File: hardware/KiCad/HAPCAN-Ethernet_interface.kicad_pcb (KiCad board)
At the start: 2 copper layers, 86.5 x 33 mm, 13 parts, among them CON1 Connectors CAN bus, IC1 MCP16301HT, U1 HLK-7628N

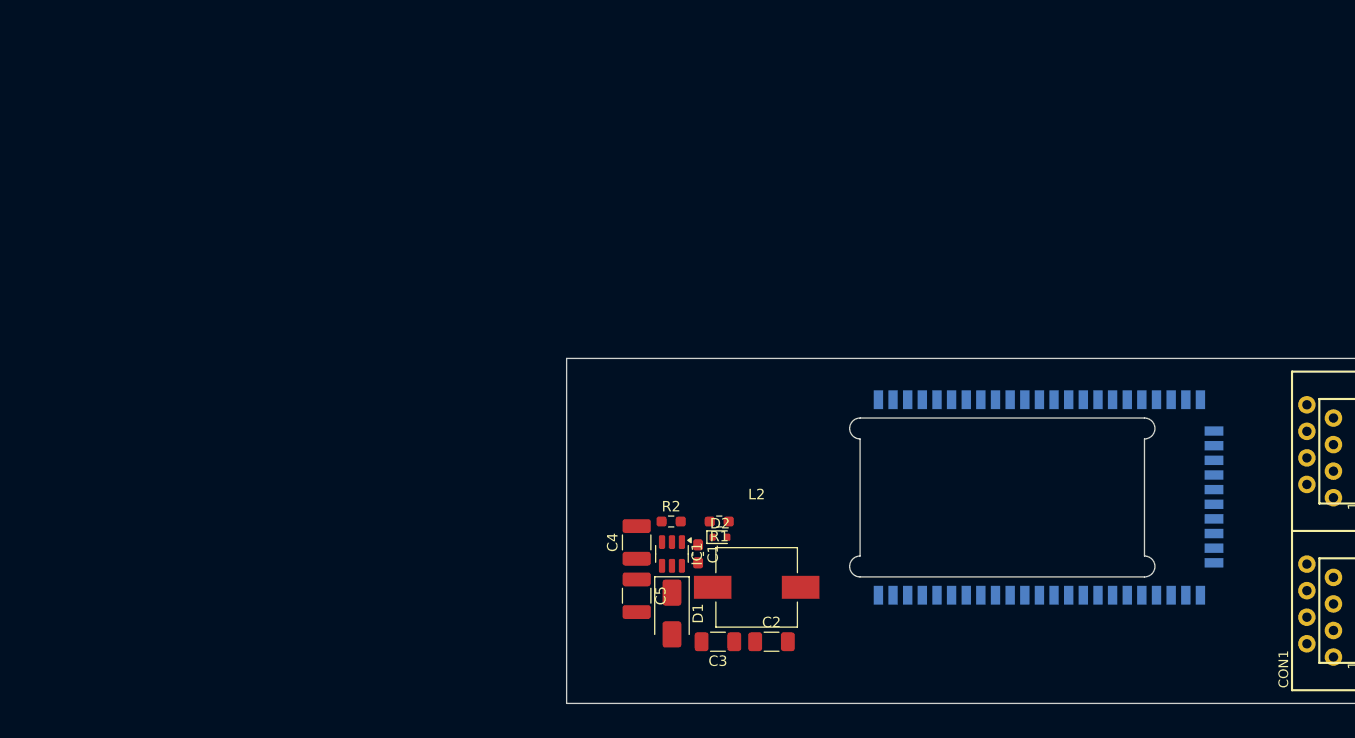
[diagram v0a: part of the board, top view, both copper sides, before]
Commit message: Made some progress in schematic, preliminary component placement on board
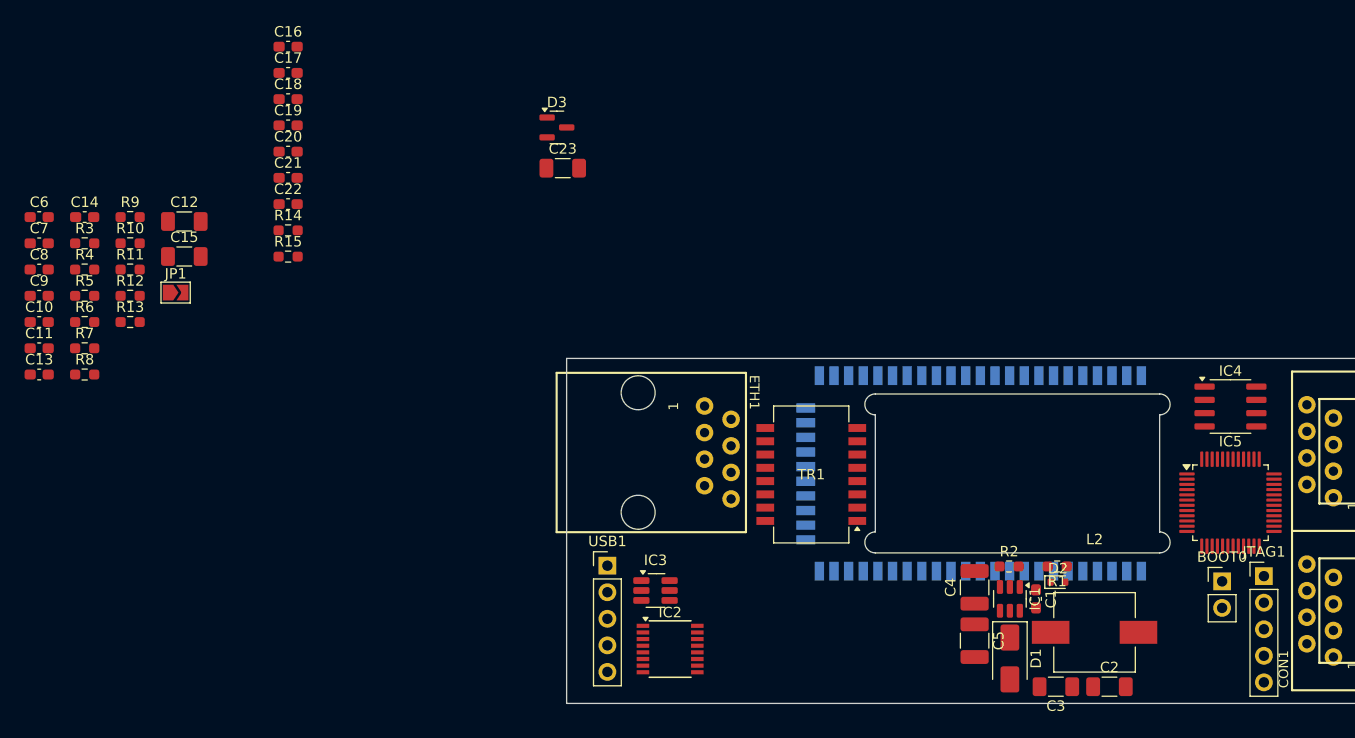
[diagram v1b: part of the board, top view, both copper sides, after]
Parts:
- added BOOT0: Jumper_2_Open, Connector_PinHeader_2.54mm:PinHeader_1x02_P2.54mm_Vertical, F.Cu at (162.7, 121.3)
- added C10: 10n, Capacitor_SMD:C_0603_1608Metric_Pad1.08x0.95mm_HandSolder, F.Cu at (49.5, 96.5)
- added C11: 100n, Capacitor_SMD:C_0603_1608Metric_Pad1.08x0.95mm_HandSolder, F.Cu at (49.5, 99.0)
- added C12: 4.7u, Capacitor_SMD:C_1206_3216Metric_Pad1.33x1.80mm_HandSolder, F.Cu at (63.4, 86.9)
- added C13: 100n, Capacitor_SMD:C_0603_1608Metric_Pad1.08x0.95mm_HandSolder, F.Cu at (49.5, 101.5)
- added C14: 100n, Capacitor_SMD:C_0603_1608Metric_Pad1.08x0.95mm_HandSolder, F.Cu at (53.9, 86.5)
- added C15: 10u, Capacitor_SMD:C_1206_3216Metric_Pad1.33x1.80mm_HandSolder, F.Cu at (63.4, 90.2)
- added C16: 100n, Capacitor_SMD:C_0603_1608Metric_Pad1.08x0.95mm_HandSolder, F.Cu at (73.4, 70.2)
- added C17: 100n, Capacitor_SMD:C_0603_1608Metric_Pad1.08x0.95mm_HandSolder, F.Cu at (73.4, 72.7)
- added C18: 100n, Capacitor_SMD:C_0603_1608Metric_Pad1.08x0.95mm_HandSolder, F.Cu at (73.4, 75.2)
- added C19: 100n, Capacitor_SMD:C_0603_1608Metric_Pad1.08x0.95mm_HandSolder, F.Cu at (73.4, 77.7)
- added C20: 100n, Capacitor_SMD:C_0603_1608Metric_Pad1.08x0.95mm_HandSolder, F.Cu at (73.4, 80.2)
- added C21: 100n, Capacitor_SMD:C_0603_1608Metric_Pad1.08x0.95mm_HandSolder, F.Cu at (73.4, 82.7)
- added C22: 100n, Capacitor_SMD:C_0603_1608Metric_Pad1.08x0.95mm_HandSolder, F.Cu at (73.4, 85.2)
- added C23: 10u 6.3V, Capacitor_SMD:C_1206_3216Metric_Pad1.33x1.80mm_HandSolder, F.Cu at (99.6, 81.8)
- added C6: 330p, Capacitor_SMD:C_0603_1608Metric_Pad1.08x0.95mm_HandSolder, F.Cu at (49.5, 86.5)
- added C7: 47p, Capacitor_SMD:C_0603_1608Metric_Pad1.08x0.95mm_HandSolder, F.Cu at (49.5, 89.0)
- added C8: 47p, Capacitor_SMD:C_0603_1608Metric_Pad1.08x0.95mm_HandSolder, F.Cu at (49.5, 91.5)
- added C9: 100n, Capacitor_SMD:C_0603_1608Metric_Pad1.08x0.95mm_HandSolder, F.Cu at (49.5, 94.0)
- added D3: SZNUP2105L, Package_TO_SOT_SMD:SOT-23, F.Cu at (99.1, 77.9)
- added ETH1: RJ45, ProjectLib:RJ45-PCB-SOCKET, F.Cu at (106.8, 109.0)
- added IC2: FT230XS, Package_SO:SSOP-16_3.9x4.9mm_P0.635mm, F.Cu at (109.9, 127.8)
- added IC3: USBLC6-2SC6, Package_TO_SOT_SMD:SOT-23-6_Handsoldering, F.Cu at (108.5, 122.2)
- added IC4: MCP2561-E-SN, Package_SO:SOIC-8_3.9x4.9mm_P1.27mm, F.Cu at (163.5, 104.6)
- added IC5: STM32F072C8Tx, Package_QFP:LQFP-48_7x7mm_P0.5mm, F.Cu at (163.5, 113.8)
- added JP1: SolderJumper_2_Open, Jumper:SolderJumper-2_P1.3mm_Open_TrianglePad1.0x1.5mm, F.Cu at (62.6, 93.7)
- added JTAG1: Conn_01x05, Connector_PinHeader_2.54mm:PinHeader_1x05_P2.54mm_Vertical, F.Cu at (166.7, 120.8)
- added R10: 27R, Resistor_SMD:R_0603_1608Metric_Pad0.98x0.95mm_HandSolder, F.Cu at (58.2, 89.0)
- added R11: 27R, Resistor_SMD:R_0603_1608Metric_Pad0.98x0.95mm_HandSolder, F.Cu at (58.2, 91.5)
- added R12: 27R, Resistor_SMD:R_0603_1608Metric_Pad0.98x0.95mm_HandSolder, F.Cu at (58.2, 94.0)
- added R13: 27R, Resistor_SMD:R_0603_1608Metric_Pad0.98x0.95mm_HandSolder, F.Cu at (58.2, 96.5)
- added R14: 10k, Resistor_SMD:R_0603_1608Metric_Pad0.98x0.95mm_HandSolder, F.Cu at (73.4, 87.8)
- added R15: 10k, Resistor_SMD:R_0603_1608Metric_Pad0.98x0.95mm_HandSolder, F.Cu at (73.4, 90.3)
- added R3: 1M, Resistor_SMD:R_0603_1608Metric_Pad0.98x0.95mm_HandSolder, F.Cu at (53.9, 89.0)
- added R4: 4k7, Resistor_SMD:R_0603_1608Metric_Pad0.98x0.95mm_HandSolder, F.Cu at (53.9, 91.5)
- added R5: 10k, Resistor_SMD:R_0603_1608Metric_Pad0.98x0.95mm_HandSolder, F.Cu at (53.9, 94.0)
- added R6: 4k7, Resistor_SMD:R_0603_1608Metric_Pad0.98x0.95mm_HandSolder, F.Cu at (53.9, 96.5)
- added R7: 10k, Resistor_SMD:R_0603_1608Metric_Pad0.98x0.95mm_HandSolder, F.Cu at (53.9, 99.0)
- added R8: 27R, Resistor_SMD:R_0603_1608Metric_Pad0.98x0.95mm_HandSolder, F.Cu at (53.9, 101.5)
- added R9: 27R, Resistor_SMD:R_0603_1608Metric_Pad0.98x0.95mm_HandSolder, F.Cu at (58.2, 86.5)
- added TR1: PT61017PEL, Transformer_SMD:Transformer_Ethernet_Bourns_PT61017PEL, F.Cu at (123.4, 111.1)
- added USB1: https://www.aliexpress.com/item/4000926155068.html, Connector_PinHeader_2.54mm:PinHeader_1x05_P2.54mm_Vertical, F.Cu at (103.9, 119.8)
- moved C2 32.6 mm to (151.9, 131.4)
- moved C3 32.6 mm to (146.8, 131.4)
- moved R1 32.6 mm to (146.9, 119.9)
- moved C4 32.6 mm to (139.0, 121.9)
- moved D2 32.6 mm to (147.0, 121.4)
- moved C1 32.6 mm to (144.9, 123.0)
- moved C5 32.6 mm to (139.0, 127.0)
- moved D1 32.6 mm to (142.4, 128.7)
- moved IC1 32.6 mm to (142.4, 123.0)
- moved L2 32.6 mm to (150.5, 126.2)
- moved R2 32.6 mm to (142.3, 119.9)
- moved U1 7.32 mm to (138.9, 111.0), turned to 0 degrees
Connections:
- net Net-(IC1-EN) renamed +24V
- U1 pad 1: Net-(U1-GND-Pad1) -> GND
- U1 pad 15: unconnected-(U1-UART_TXD1-Pad15) -> Net-(U1-UART_TXD1)
- U1 pad 16: unconnected-(U1-UART_RXD1-Pad16) -> Net-(U1-UART_RXD1)
- U1 pad 2: unconnected-(U1-3.3VD-Pad2) -> +3V3
- U1 pad 21: Net-(U1-GND-Pad1) -> GND
- U1 pad 23: Net-(U1-GND-Pad1) -> GND
- U1 pad 3: unconnected-(U1-3.3VD-Pad3) -> +3V3
- U1 pad 31: unconnected-(U1-UART_TXD0-Pad31) -> Net-(U1-UART_TXD0)
- U1 pad 32: unconnected-(U1-UART_RXD0-Pad32) -> Net-(U1-UART_RXD0)
- U1 pad 34: unconnected-(U1-MDI_RP_P0-Pad34) -> /PHY_RX+
- U1 pad 35: unconnected-(U1-MDI_RN_P0-Pad35) -> /PHY_RX-
- U1 pad 36: unconnected-(U1-MDI_TP_P0-Pad36) -> /PHY_TX+
- U1 pad 37: unconnected-(U1-MDI_TN_P0-Pad37) -> /PHY_TX-
- U1 pad 4: Net-(U1-GND-Pad1) -> GND
- U1 pad 56: Net-(U1-GND-Pad1) -> GND

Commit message: Finished schematic, but needs cleanup. Started component placement on board.
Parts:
- removed D2: BAS521-QX, Diode_SMD:D_SOD-523
- added C15: 100n, Capacitor_SMD:C_0603_1608Metric_Pad1.08x0.95mm_HandSolder, B.Cu at (172.5, 117.6)
- added C16: 10u 16V, Capacitor_SMD:C_1210_3225Metric_Pad1.33x2.70mm_HandSolder, F.Cu at (70.3, 167.6)
- added C17: 10u 10V, Capacitor_SMD:C_1210_3225Metric_Pad1.33x2.70mm_HandSolder, F.Cu at (77.3, 160.9)
- added C18: 22u 10V, Capacitor_SMD:C_1210_3225Metric_Pad1.33x2.70mm_HandSolder, F.Cu at (80.6, 160.9)
- added C20: 10n, Capacitor_SMD:C_0603_1608Metric_Pad1.08x0.95mm_HandSolder, F.Cu at (137.0, 183.0)
- added C21: 100n, Capacitor_SMD:C_0603_1608Metric_Pad1.08x0.95mm_HandSolder, F.Cu at (139.5, 183.7)
- added C22: 10u 6.3V, Capacitor_SMD:C_1206_3216Metric_Pad1.33x1.80mm_HandSolder, F.Cu at (135.0, 183.9)
- added C23: 100n, Capacitor_SMD:C_0603_1608Metric_Pad1.08x0.95mm_HandSolder, F.Cu at (137.2, 179.6)
- added C24: 100n, Capacitor_SMD:C_0603_1608Metric_Pad1.08x0.95mm_HandSolder, F.Cu at (145.2, 179.6)
- added C6: 100n, Capacitor_SMD:C_0603_1608Metric_Pad1.08x0.95mm_HandSolder, F.Cu at (57.0, 162.7)
- added C7: 100n, Capacitor_SMD:C_0603_1608Metric_Pad1.08x0.95mm_HandSolder, F.Cu at (67.9, 161.6)
- added C8: 10u 16V, Capacitor_SMD:C_1210_3225Metric_Pad1.33x2.70mm_HandSolder, F.Cu at (70.3, 162.6)
- added FB1: 1k@100MHz, Inductor_SMD:L_0805_2012Metric_Pad1.15x1.40mm_HandSolder, F.Cu at (160.0, 127.9)
- added FB2: 1k@100MHz, Inductor_SMD:L_0805_2012Metric_Pad1.15x1.40mm_HandSolder, F.Cu at (165.2, 131.3)
- added IC3: TLV62568DRL, Package_TO_SOT_SMD:SOT-563, F.Cu at (73.3, 164.2)
- added IC5: MCP3422A0-E/MS, Package_SO:MSOP-8_3x3mm_P0.65mm, F.Cu at (141.2, 181.1)
- added L1: 3.3uH, ProjectLib:SPM7054VT, F.Cu at (63.5, 165.2)
- added NT1: NetTie_2, NetTie:NetTie-2_SMD_Pad0.5mm, F.Cu at (58.9, 155.3)
- added NT2: NetTie_2, NetTie:NetTie-2_SMD_Pad0.5mm, F.Cu at (55.8, 155.3)
- added NT3: NetTie_2, NetTie:NetTie-2_SMD_Pad0.5mm, F.Cu at (83.0, 162.5)
- added NT4: NetTie_2, NetTie:NetTie-2_SMD_Pad0.5mm, F.Cu at (83.0, 161.6)
- added R10: 22k, Resistor_SMD:R_0603_1608Metric_Pad0.98x0.95mm_HandSolder, F.Cu at (146.7, 179.6)
- added R13: 10k, Resistor_SMD:R_0603_1608Metric_Pad0.98x0.95mm_HandSolder, B.Cu at (119.8, 119.9)
- added R14: 10k, Resistor_SMD:R_0603_1608Metric_Pad0.98x0.95mm_HandSolder, B.Cu at (118.3, 119.9)
- added R3: 100k, Resistor_SMD:R_0603_1608Metric_Pad0.98x0.95mm_HandSolder, F.Cu at (73.6, 162.3)
- added R4: 22k, Resistor_SMD:R_0603_1608Metric_Pad0.98x0.95mm_HandSolder, F.Cu at (73.6, 160.8)
- added R7: 330k, Resistor_SMD:R_0603_1608Metric_Pad0.98x0.95mm_HandSolder, F.Cu at (134.2, 179.6)
- added R8: 22k, Resistor_SMD:R_0603_1608Metric_Pad0.98x0.95mm_HandSolder, F.Cu at (135.7, 179.6)
- added R9: 22k, Resistor_SMD:R_0603_1608Metric_Pad0.98x0.95mm_HandSolder, F.Cu at (148.2, 179.6)
- added TVS1: P6SMB33CA, Diode_SMD:D_SMB_Handsoldering, F.Cu at (166.9, 125.3)
- C2: value 10u 6.3V -> 100n; footprint Capacitor_SMD:C_1206_3216Metric_Pad1.33x1.80mm_HandSolder -> Capacitor_SMD:C_0603_1608Metric_Pad1.08x0.95mm_HandSolder
- C3: value 10u 6.3V -> 10u 10V
- C35: renamed from C6; moved to B.Cu
- D1: value B140Q -> US1D; footprint Diode_SMD:D_SMA -> Diode_SMD:D_SMA_Handsoldering
- IC1: value MCP16301HT -> LMR51430Y
- L2: value 15uH -> 1uH; footprint Inductor_SMD:L_Wuerth_WE-PD-Typ-M-Typ-S_Handsoldering -> ProjectLib:SPM7054VT
- R1: value 31k6 -> 200k
- R2: value 10k -> 27k
- TVS2: renamed from D3; moved to B.Cu
- moved C1 99.1 mm to (56.4, 167.7), turned to 0 degrees
- moved R2 98.5 mm to (54.0, 163.5), turned to 90 degrees
- moved IC1 95.4 mm to (56.8, 165.2), turned to 180 degrees
- moved R1 92.5 mm to (63.9, 160.8)
- moved C4 89.0 mm to (57.3, 157.1), turned to 180 degrees
- moved C5 88.2 mm to (57.3, 160.3), turned to 180 degrees
- moved L2 83.0 mm to (78.3, 167.1)
- moved TVS2 81.5 mm to (171.6, 115.0)
- moved C10 76.4 mm to (148.7, 87.9)
- moved C11 76.4 mm to (148.7, 90.4)
- moved C12 76.4 mm to (148.7, 92.9)
- moved C13 76.4 mm to (148.7, 95.4)
- moved C9 76.4 mm to (148.7, 97.9)
- moved C29 73.7 mm to (114.9, 128.1), turned to 90 degrees
- moved C28 71.1 mm to (124.6, 119.5), turned to 180 degrees
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- renumbered BOOT0 to BOOT1, C18 to C10, C19 to C11, C20 to C12, C21 to C13, C23 to C14, C17 to C19, C13 to C25, C14 to C26, C15 to C27, C16 to C28, C9 to C29, C11 to C30, C12 to C31, C10 to C32, C7 to C33, C8 to C34, C22 to C9, IC4 to IC2, IC5 to IC4, IC3 to IC6, IC2 to IC7, R12 to R11, R13 to R12, R10 to R15, R11 to R16, R8 to R17, R9 to R18, R3 to R19, R4 to R20, R6 to R21, R5 to R22, R7 to R23, R15 to R5, R14 to R6
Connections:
- C1 pad 1: Net-(D2-K) -> Net-(IC1-CB)
- C1 pad 2: Net-(D1-K) -> Net-(IC1-SW)
- C2 pad 1: +3V3 -> +5V
- C3 pad 1: +3V3 -> +5V
- CON1 pad +24V: unconnected-(CON1-Pad+24V) -> Net-(D1-A)
- CON1 pad CANH: unconnected-(CON1-PadCANH) -> /CANH
- CON1 pad CANL: unconnected-(CON1-PadCANL) -> /CANL
- CON1 pad GND: unconnected-(CON1-PadGND) -> GNDPWR
- D1 pad 2: GND -> Net-(D1-A)
- IC1 pad 1: Net-(D2-K) -> GND
- IC1 pad 2: GND -> Net-(IC1-SW)
- IC1 pad 3: Net-(IC1-Vfb) -> +24V
- IC1 pad 4: +24V -> Net-(IC1-FB)
- IC1 pad 6: Net-(D1-K) -> Net-(IC1-CB)
- IC2 pad 1: unconnected-(IC4-TXD-Pad1) -> /CAN_Tx
- IC2 pad 2: unconnected-(IC4-VSS-Pad2) -> GND
- IC2 pad 3: unconnected-(IC4-VDD-Pad3) -> +5V
- IC2 pad 4: unconnected-(IC4-RXD-Pad4) -> /CAN_Rx
- IC2 pad 6: unconnected-(IC4-CANL-Pad6) -> /CANL
- IC2 pad 7: unconnected-(IC4-CANH-Pad7) -> /CANH
- IC2 pad 8: unconnected-(IC4-STBY-Pad8) -> GND
- IC4 pad 32: unconnected-(IC5-PA11-Pad32) -> /CAN_USB_D-
- IC4 pad 33: unconnected-(IC5-PA12-Pad33) -> /CAN_USB_D+
- IC4 pad 34: unconnected-(IC5-PA13-Pad34) -> /SWDIO
- IC4 pad 37: unconnected-(IC5-PA14-Pad37) -> /SWCLK
- IC4 pad 45: unconnected-(IC5-PB8-Pad45) -> /CAN_Rx
- IC4 pad 46: unconnected-(IC5-PB9-Pad46) -> /CAN_Tx
- IC6 pad 1: Net-(USB1-D+) -> Net-(USB1-D-)
- IC6 pad 3: Net-(USB1-D-) -> Net-(USB1-D+)
- L2 pad 1: Net-(D1-K) -> Net-(IC3-SW)
- R1 pad 1: +3V3 -> +5V
- R1 pad 2: Net-(IC1-Vfb) -> Net-(IC1-FB)
- R17 pad 2: /D+ -> /D-
- R18 pad 2: /D- -> /D+
- R2 pad 1: Net-(IC1-Vfb) -> Net-(IC1-FB)
- TVS2 pad 1: unconnected-(D3-K-Pad1) -> /CANH
- TVS2 pad 2: unconnected-(D3-K-Pad2) -> /CANL
- TVS2 pad 3: unconnected-(D3-A-Pad3) -> GNDPWR
- U1 pad 24: unconnected-(U1-I2C_SCLK-Pad24) -> /I2C_CLK
- U1 pad 25: unconnected-(U1-I2C_SD-Pad25) -> /I2C_SDA
- U1 pad 54: unconnected-(U1-USB_DP-Pad54) -> /CAN_USB_D+
- U1 pad 55: unconnected-(U1-USB_DM-Pad55) -> /CAN_USB_D-

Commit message: Did some work on board.
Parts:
- C2, C3, D1, FB1, FB2, IC2, TVS1: moved to B.Cu
- TVS2: footprint Package_TO_SOT_SMD:SOT-23 -> Package_TO_SOT_SMD:SOT-23-3; moved to F.Cu
- moved C14 116.2 mm to (71.8, 168.4)
- moved C1 115.5 mm to (159.1, 114.8)
- moved C4 115.5 mm to (160.0, 104.2)
- moved C5 115.5 mm to (160.0, 107.4)
- moved IC1 115.5 mm to (159.5, 112.3)
- moved C6 115.5 mm to (159.7, 109.8)
- moved R2 115.5 mm to (156.7, 110.6)
- moved L1 113.8 mm to (165.2, 114.1), turned to -90 degrees
- moved NT2 112.6 mm to (157.8, 107.6), turned to 180 degrees
- moved NT1 111.7 mm to (160.1, 108.1), turned to 180 degrees
- moved R1 104.0 mm to (156.7, 113.9), turned to 90 degrees
- moved C7 102.5 mm to (159.9, 116.3), turned to 0 degrees
- moved C8 101.8 mm to (162.8, 120.1), turned to 0 degrees
- moved IC4 100.7 mm to (81.7, 169.6)
- moved C16 100.6 mm to (158.7, 119.6)
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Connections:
- TVS2 pad 1: /CANH -> /CANL
- TVS2 pad 2: /CANL -> /CANH
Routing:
- net GNDPWR: track 0.00 -> 71.7 mm, vias 0 -> 9
- net Net-(D1-A): track 0.00 -> 54.1 mm
- net GND: track 0.00 -> 51.7 mm, vias 0 -> 46
- net /CANL: track 0.00 -> 37.7 mm, vias 0 -> 1
- net VBUS: track 0.00 -> 36.4 mm, vias 0 -> 2
- net /CANH: track 0.00 -> 30.0 mm, vias 0 -> 1
- net Net-(U1-UART_RXD0): track 0.00 -> 18.7 mm, vias 0 -> 1
- net Net-(U1-UART_TXD0): track 0.00 -> 18.5 mm, vias 0 -> 1
- net +3V3: track 0.00 -> 18.1 mm
- net /PHY_TX-: track 0.00 -> 15.0 mm, vias 0 -> 1
- net Net-(TR1-C_RD): track 0.00 -> 14.6 mm
- net /PHY_TX+: track 0.00 -> 13.6 mm, vias 0 -> 1
- net /UART_FTDI_Tx: track 0.00 -> 12.7 mm, vias 0 -> 3
- net Net-(USB1-D-): track 0.00 -> 12.4 mm, vias 0 -> 2
- net Net-(USB1-D+): track 0.00 -> 9.75 mm
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- added copper zone on F.Cu, net +24V
- added copper zone on F.Cu, net +5V
- added copper zone on B.Cu, net GND
- added copper zone on F.Cu, net GND
- added copper zone on B.Cu, net GNDPWR
- added copper zone on F.Cu, net Net-(IC1-SW)

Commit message: Placed almost all footprints on the PCB
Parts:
- C2, C3, IC2: moved to F.Cu
- C25, C26, C27: moved to B.Cu
- moved C25 106.2 mm to (153.5, 123.4)
- moved C26 103.1 mm to (150.2, 123.4), turned to 180 degrees
- moved C27 93.6 mm to (150.2, 125.3), turned to 180 degrees
- moved C19 81.1 mm to (138.0, 121.6)
- moved R6 80.3 mm to (142.9, 128.0), turned to -90 degrees
- moved IC4 69.5 mm to (137.0, 127.5)
- moved C14 69.3 mm to (130.7, 131.8), turned to 180 degrees
- moved R5 67.3 mm to (132.3, 122.7), turned to -90 degrees
- moved R9 63.1 mm to (119.9, 123.2), turned to 0 degrees
- moved BOOT1 62.1 mm to (129.6, 123.5)
- moved R10 60.7 mm to (119.0, 125.6), turned to -90 degrees
- moved C24 59.4 mm to (120.5, 125.6), turned to 90 degrees
- moved IC5 56.7 mm to (123.0, 127.4), turned to 90 degrees
- moved C21 56.1 mm to (127.0, 129.0), turned to 90 degrees
- moved C20 55.2 mm to (125.5, 129.0), turned to 90 degrees
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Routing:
- net /CANH: track 30.0 -> 55.9 mm, vias 1 -> 2
- net /CANL: track 37.7 -> 62.9 mm, vias 1 -> 2
- net /I2C_SDA: track 4.31 -> 19.7 mm, vias 0 -> 1
- net /BOOT0: track 0.00 -> 13.7 mm, vias 0 -> 1
- net /CAN_Tx: track 0.00 -> 12.8 mm, vias 0 -> 2
- net /CAN_Rx: track 0.00 -> 9.69 mm
- net /NRST: track 0.00 -> 8.66 mm
- net +3V3: track 18.1 -> 26.5 mm
- net /I2C_CLK: track 2.23 -> 9.85 mm, vias 0 -> 1
- net Net-(IC5-CH1+): track 0.00 -> 6.60 mm, vias 0 -> 2
- net Net-(IC5-CH2+): track 0.00 -> 6.06 mm
- net /ADC_GND: track 0.00 -> 5.38 mm
- net /ADC_GND2: track 0.00 -> 3.53 mm
- net GND: track 51.7 -> 48.3 mm, vias 46 -> 47
- net Net-(IC3-FB): track 0.00 -> 2.84 mm
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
